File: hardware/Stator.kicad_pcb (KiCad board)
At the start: 2 copper layers, 200 x 200 mm, 0 parts

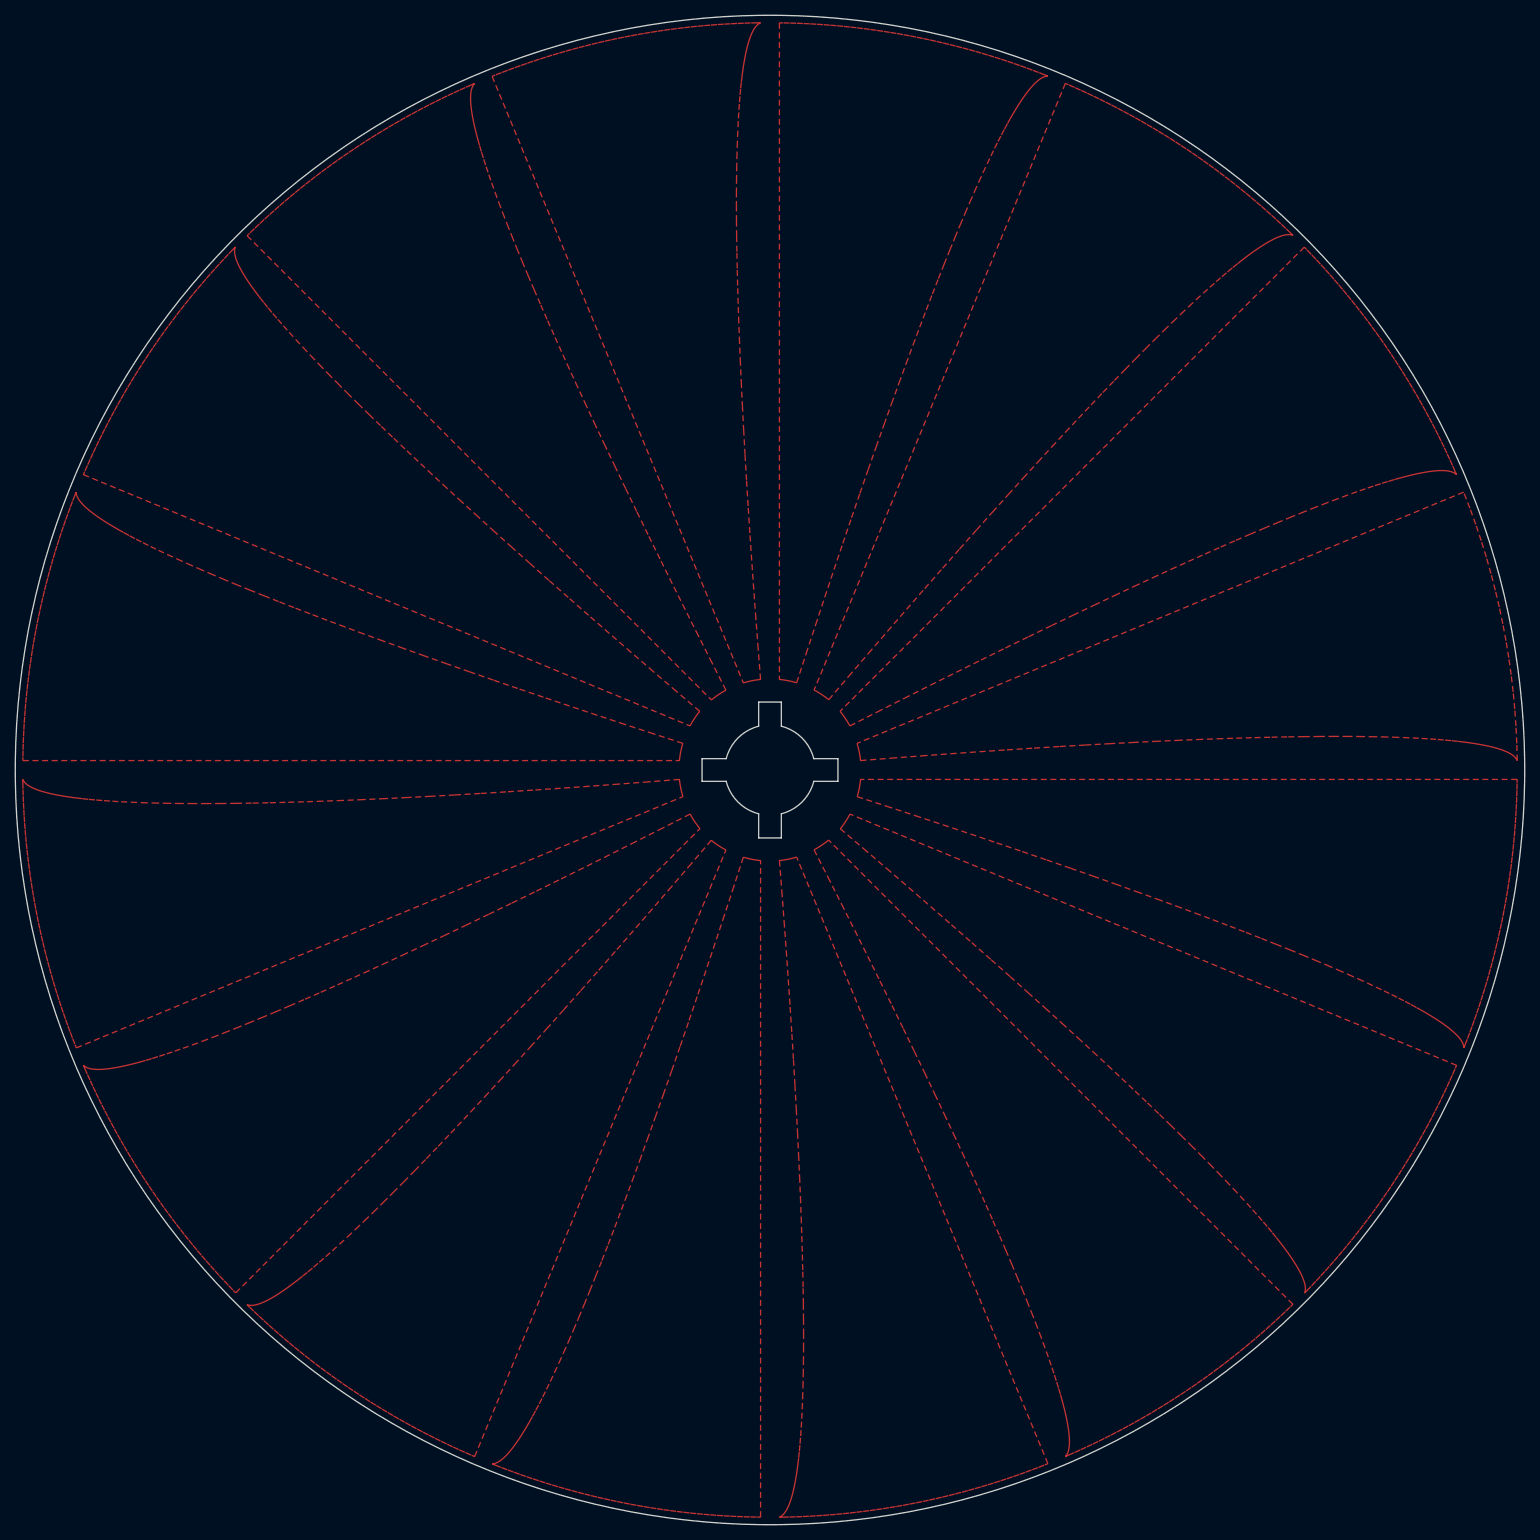
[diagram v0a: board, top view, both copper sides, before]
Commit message: Generator design
Updated the rotor design.
Updated the stator design.
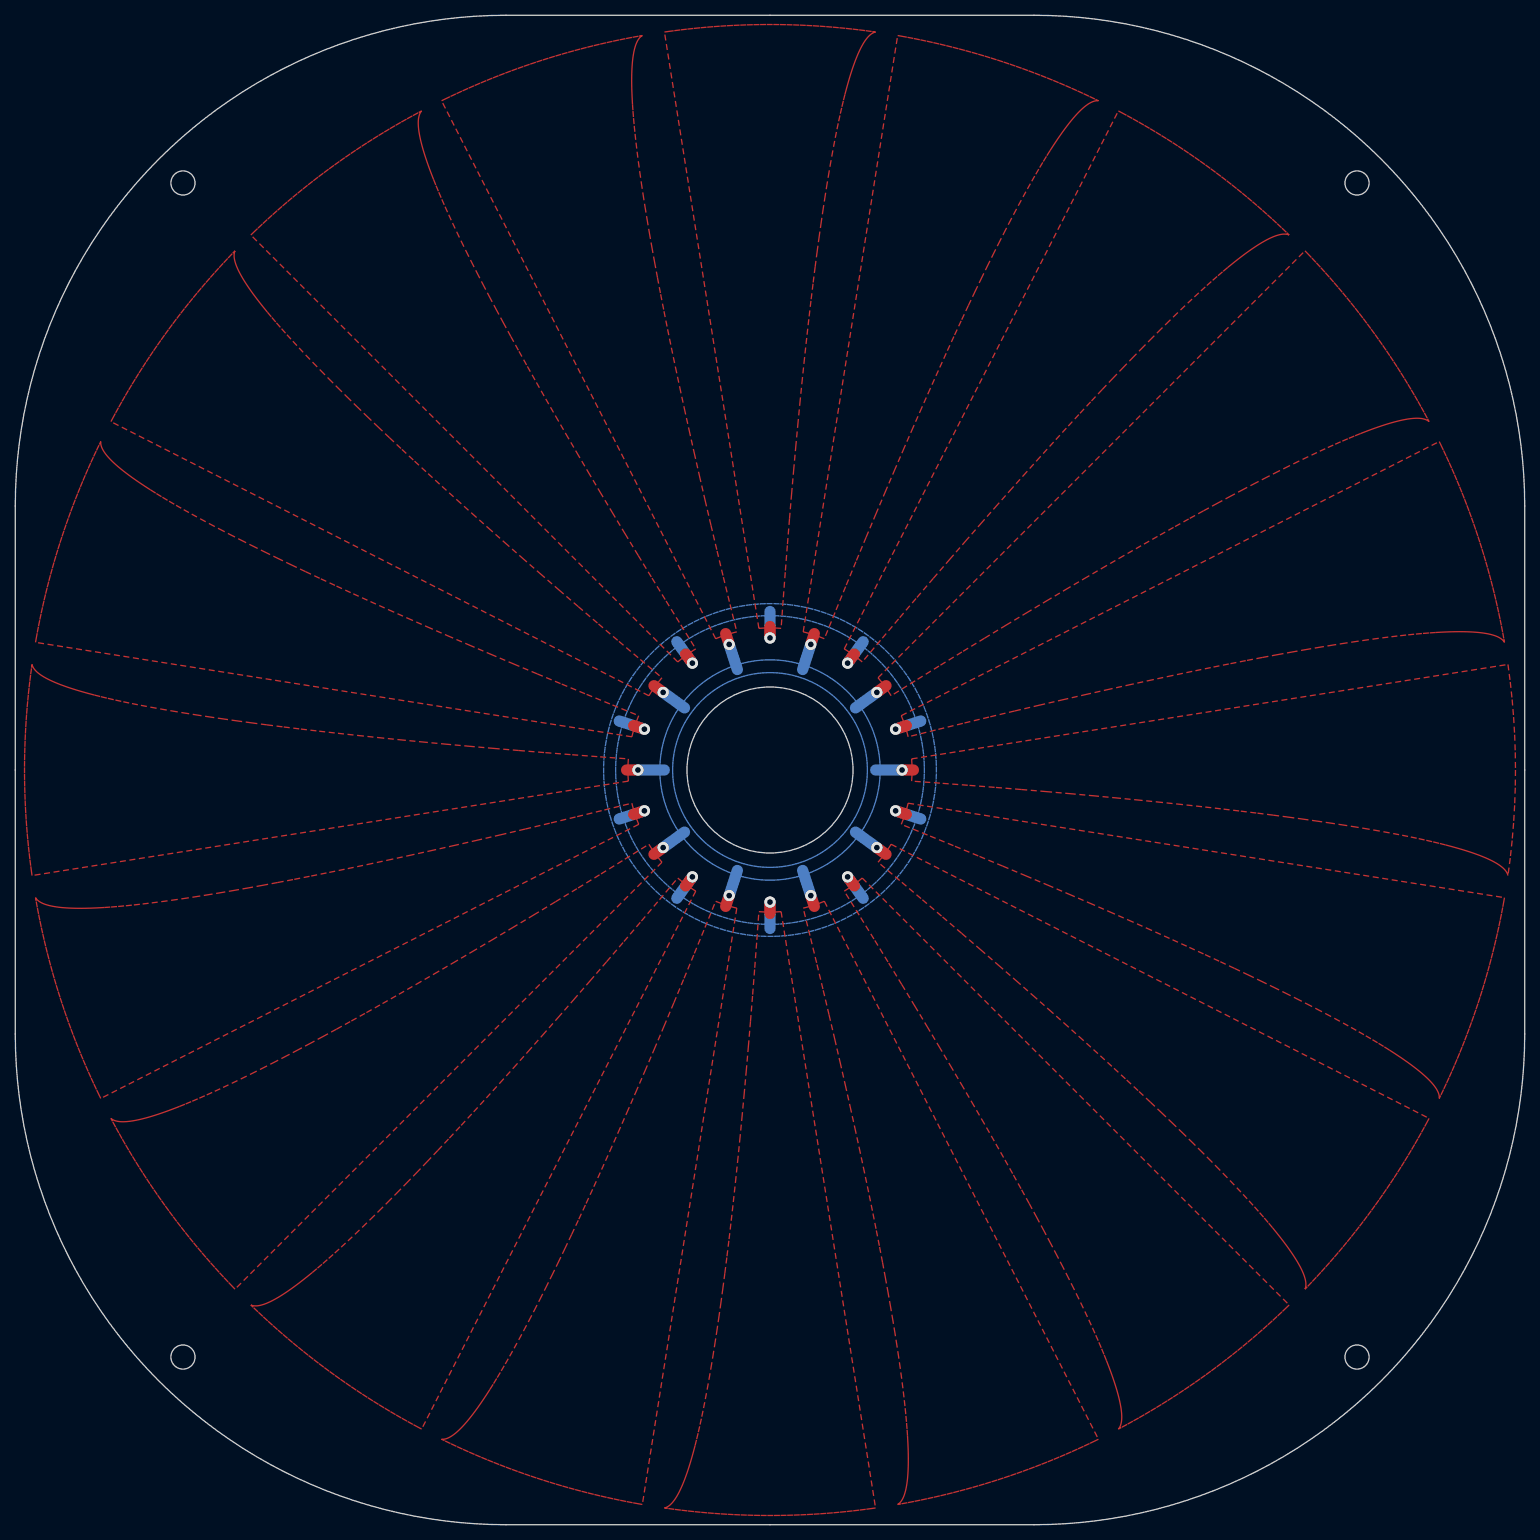
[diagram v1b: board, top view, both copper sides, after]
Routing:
- net B: track 0.00 -> 50.0 mm, vias 0 -> 10
- net A: track 0.00 -> 50.0 mm, vias 0 -> 10
- added copper zone on B.Cu, net A
- added copper zone on F.Cu, net A
- added copper zone on B.Cu, net B
- added copper zone on F.Cu, net B
- removed copper zone on F.Cu, net (none)
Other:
- outline, holes or cut-outs redrawn

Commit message: Libraries and generator design
Updated the generator design.
Added a libraries folder.
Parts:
- added G***: LOGO, TENG:QR, B.Cu at (200.0, 207.0)
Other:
- board text added: "PD 11/01/26"
- board text added: "REV A"
- board text added: "SLIDING TENG"
- board text added: "VERSION 1.0"

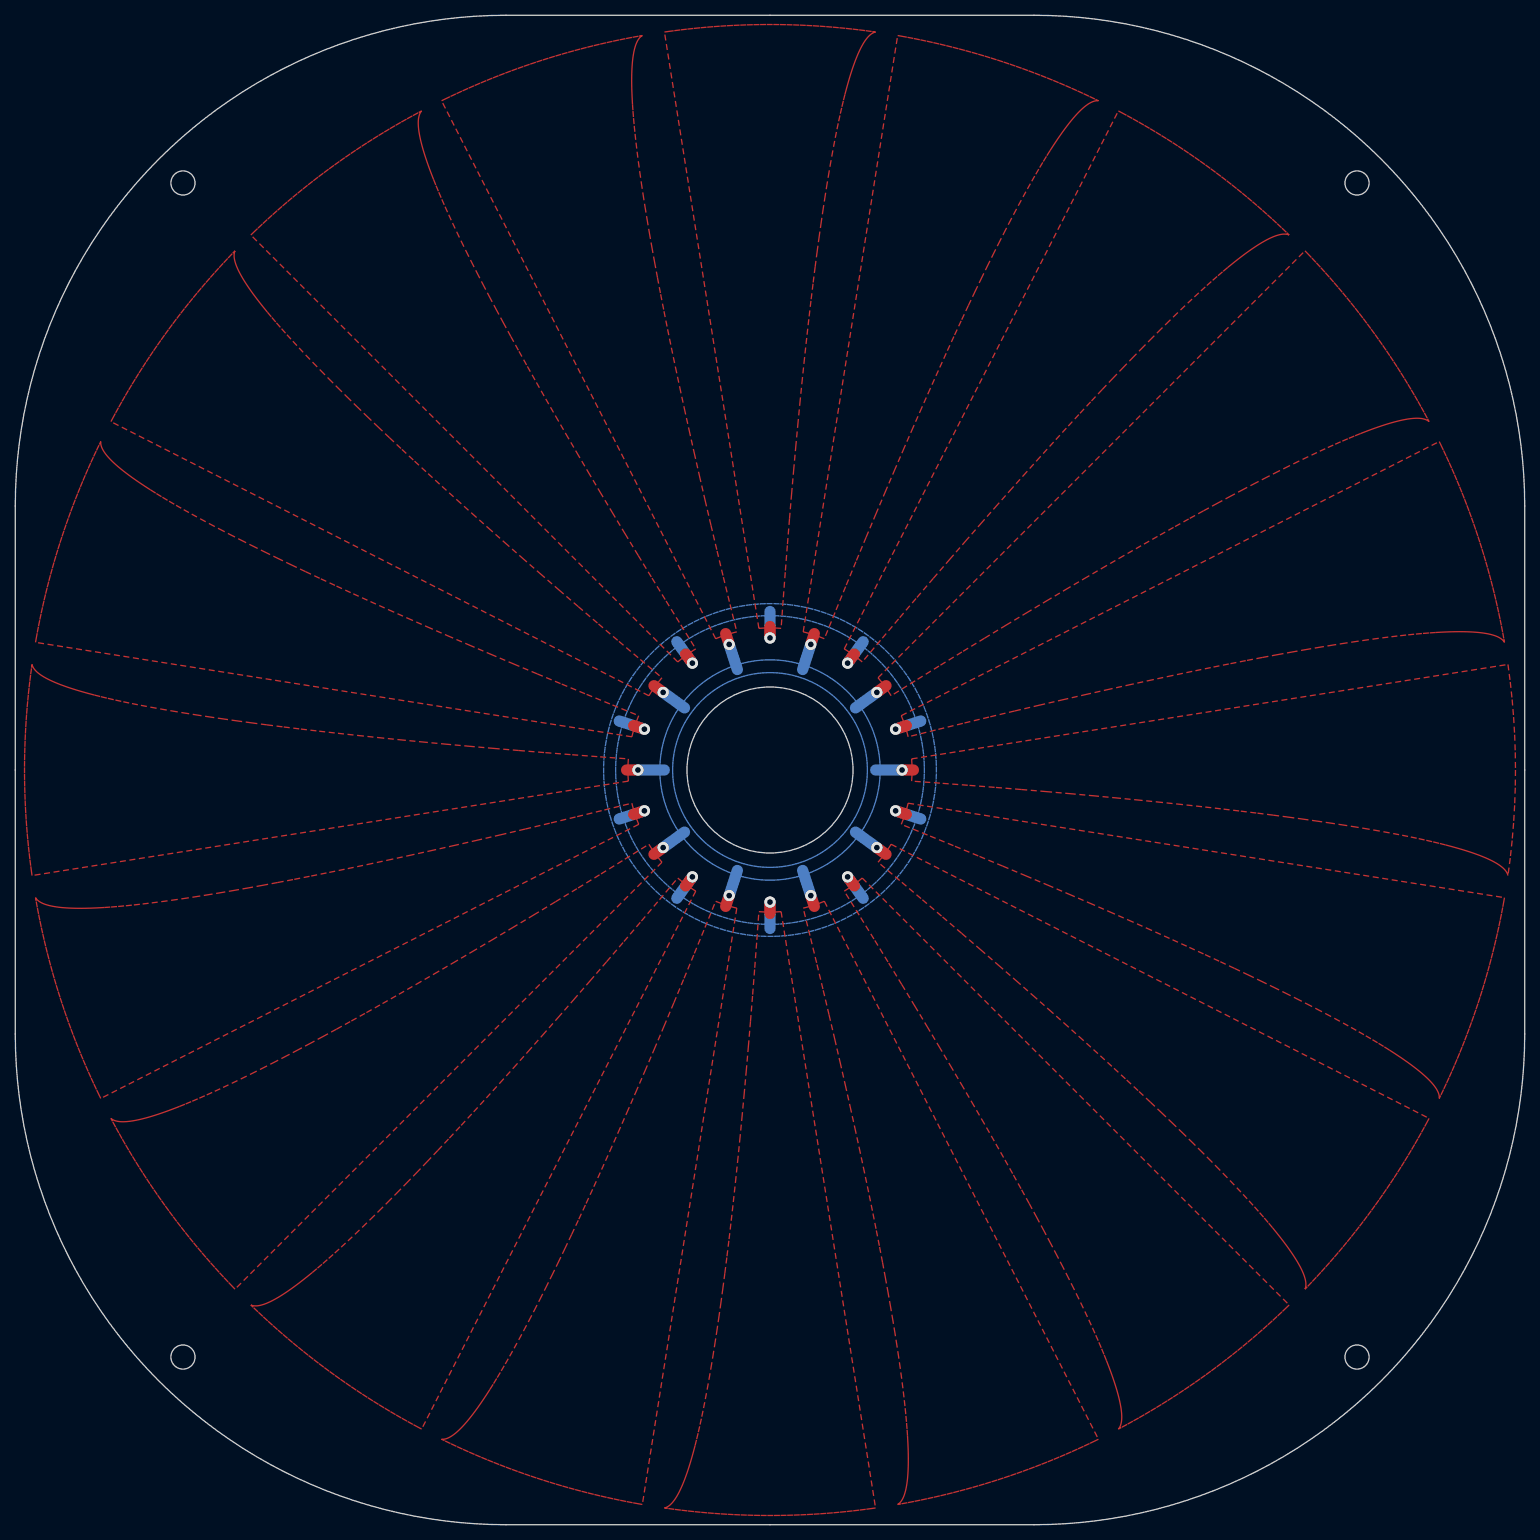
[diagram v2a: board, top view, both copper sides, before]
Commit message: Generator design
Updated the rotor board design.
Updated the stator board design.
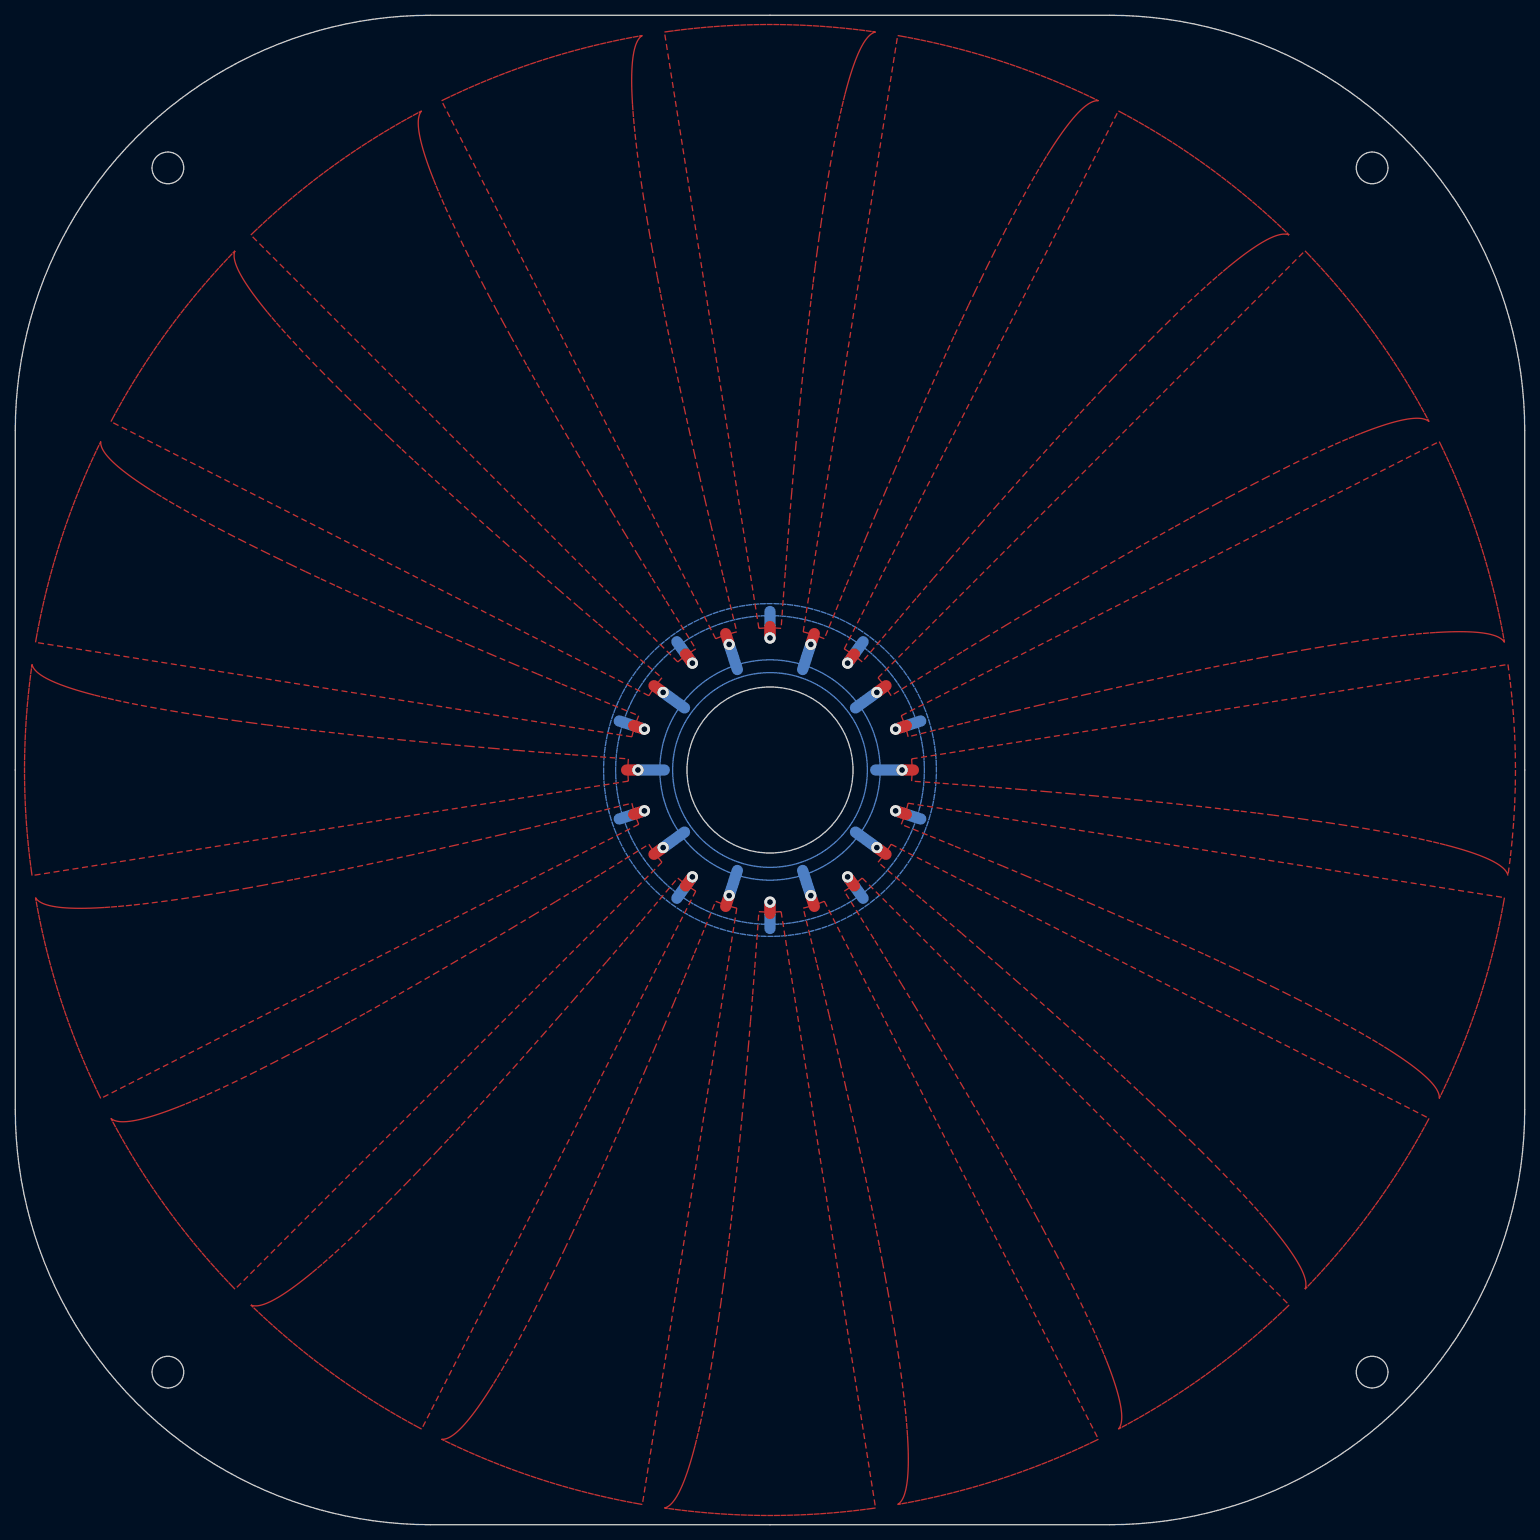
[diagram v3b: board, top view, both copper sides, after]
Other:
- outline, holes or cut-outs redrawn
- board text added: "TENG STATOR"
- board text removed: "SLIDING TENG"
